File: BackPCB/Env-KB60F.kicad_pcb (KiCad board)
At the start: 2 copper layers, 283 x 126.5 mm, 9 parts

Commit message: Moved MCU lower to allow for mount hole to fit properly, Generated Gerber and bottom plate Gerber
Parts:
- G***: moved to B.Cu
- moved H11 1.75 mm to (353.1, 36.5)
- turned G*** to 180 degrees
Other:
- net class DIFF removed
- net class USB added: clearance 0.2, trace_width 0.25, via_dia 0.8, via_drill 0.4
- board text added: "Envious.Media"
- board text removed: "Envious.Media 2021"
- board text removed: "http://github.com/envious-data/env-kb60f"

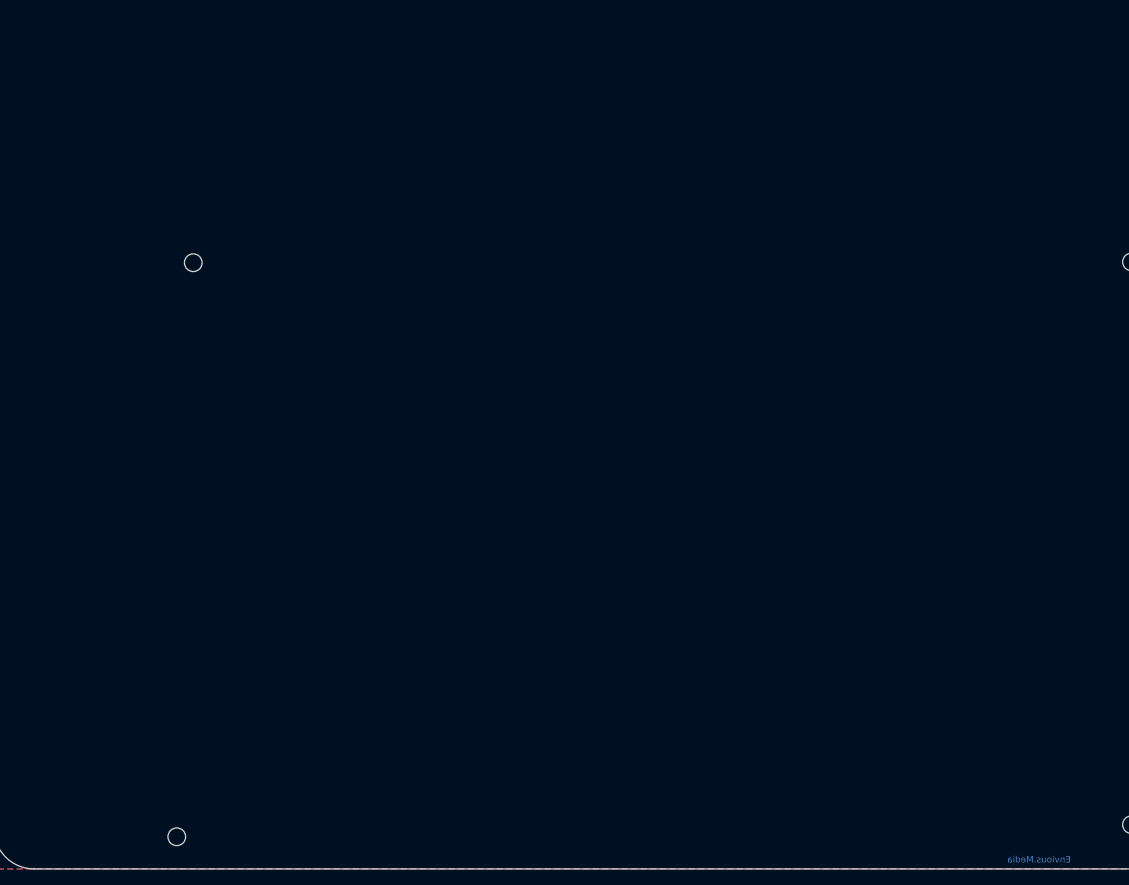
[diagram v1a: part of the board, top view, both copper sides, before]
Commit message: Corrected silkscreen, Generated updated Gerbers
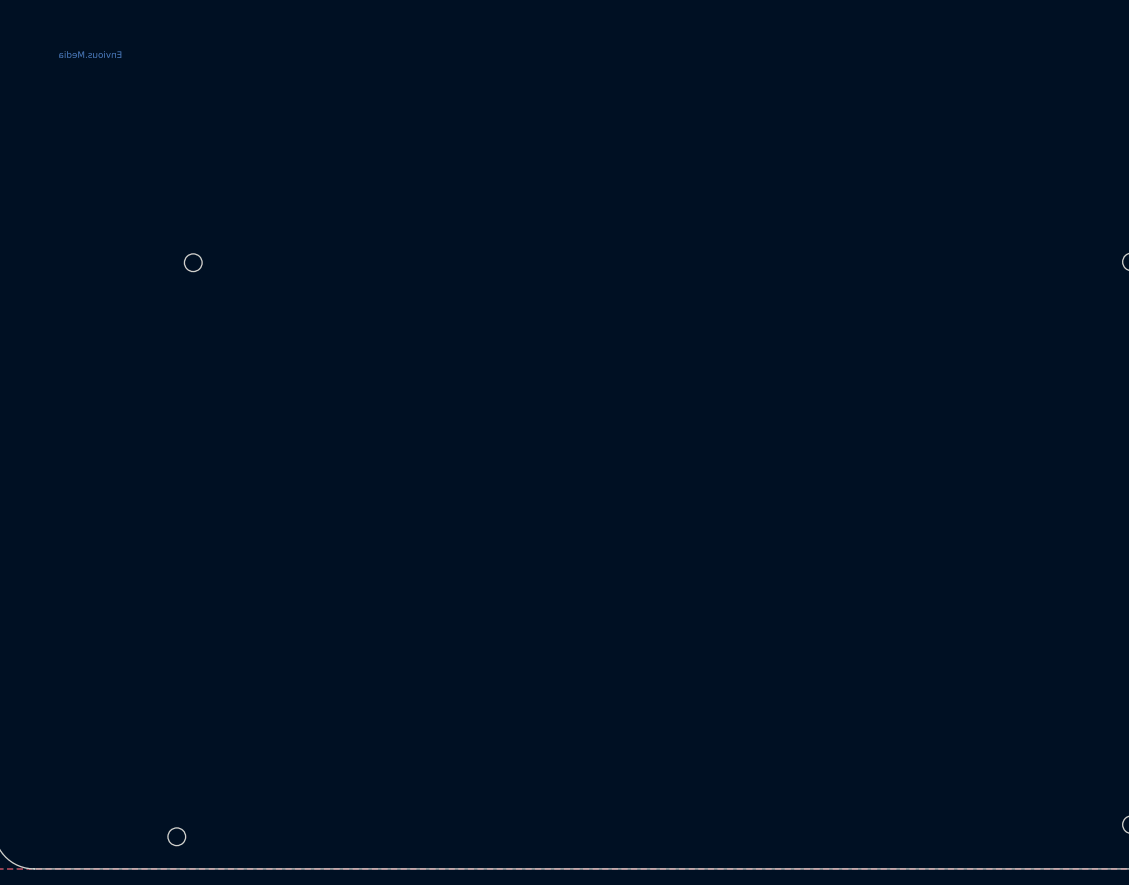
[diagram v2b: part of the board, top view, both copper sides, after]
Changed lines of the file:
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@@
     (pcbplotparams
       (layerselection 0x010fc_ffffffff)
-      (usegerberextensions false)
+      (usegerberextensions true)
       (usegerberattributes false)
       (usegerberadvancedattributes false)
@@
       (plotinvisibletext false)
       (padsonsilk false)
-      (subtractmaskfromsilk false)
+      (subtractmaskfromsilk true)
       (outputformat 1)
       (mirror false)
@@
     (effects (font (size 1.75 1.75) (thickness 0.15)) (justify mirror))
   )
-  (gr_text Envious.Media (at 207 158.325) (layer B.Cu)
+  (gr_text Envious.Media (at 89 58.25) (layer B.Cu)
     (effects (font (size 0.8 0.8) (thickness 0.15)) (justify mirror))
   )

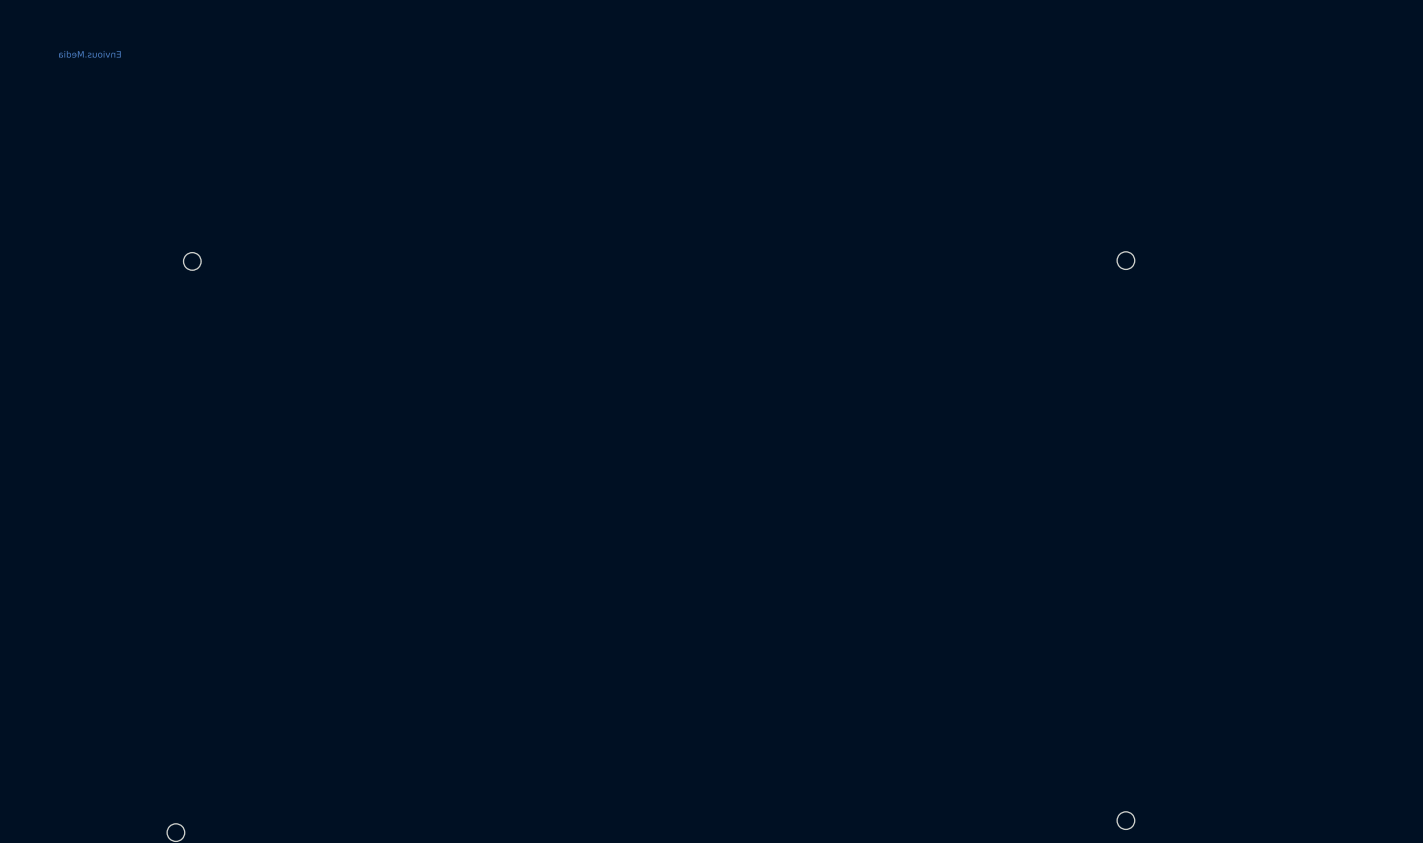
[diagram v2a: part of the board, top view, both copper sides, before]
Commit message: fixed backplate's ground fill and added a center logo on the rear of it.
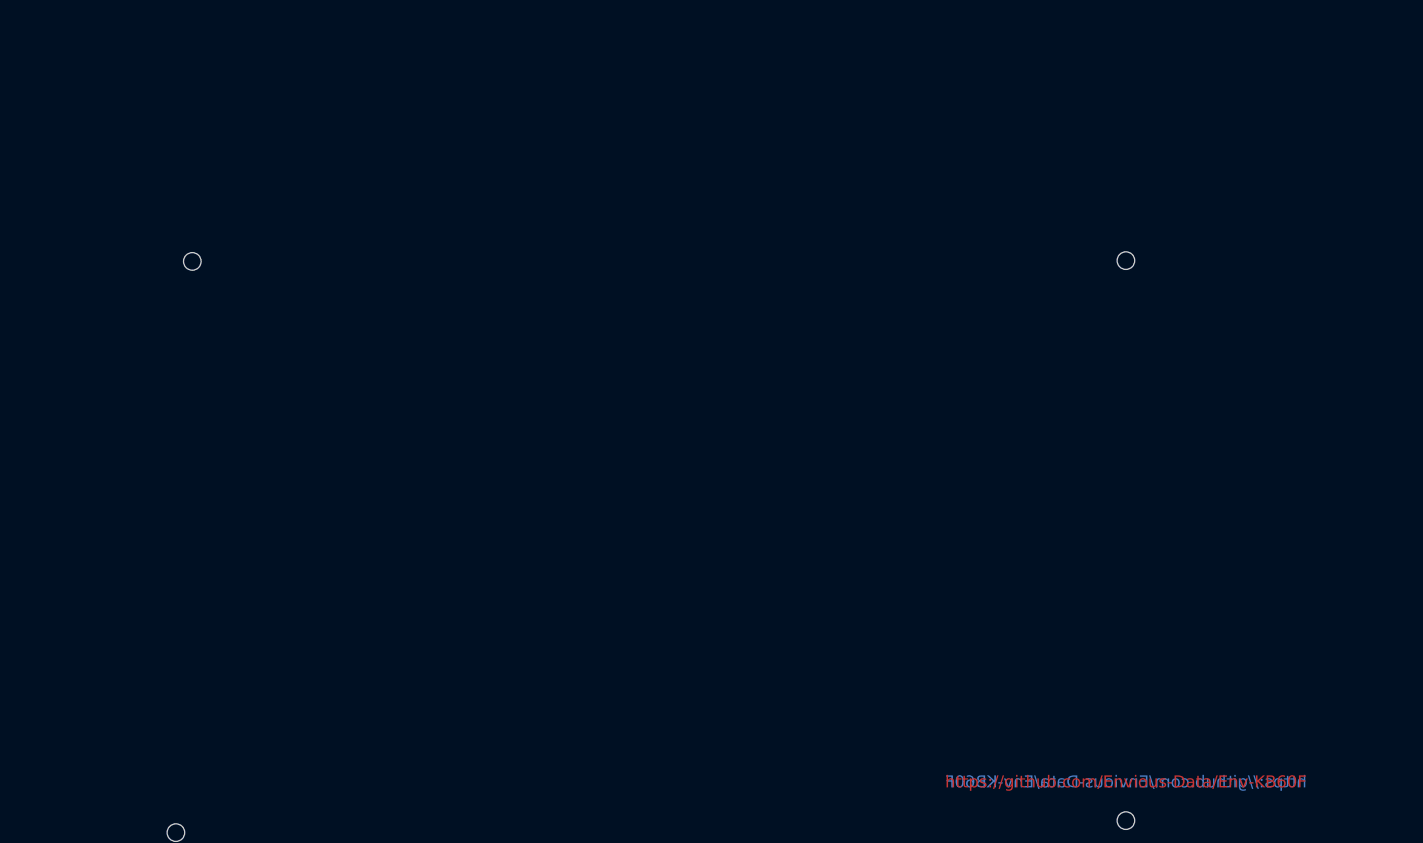
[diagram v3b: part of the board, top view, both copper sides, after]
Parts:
- removed the G*** at (87.2, 47.5)
- added G***: LOGO, Logo:logo, B.Cu at (218.5, 92.3)
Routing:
- added copper zone on B.Cu, net (none)
- added copper zone on F.Cu, net (none)
- removed copper zone on B.Cu, net GND
- removed copper zone on F.Cu, net GND
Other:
- board text added: "https://github.com/Envious-Data/Env-KB60F"
- board text removed: "Env-KB60F"
- board text removed: "Envious.Media"

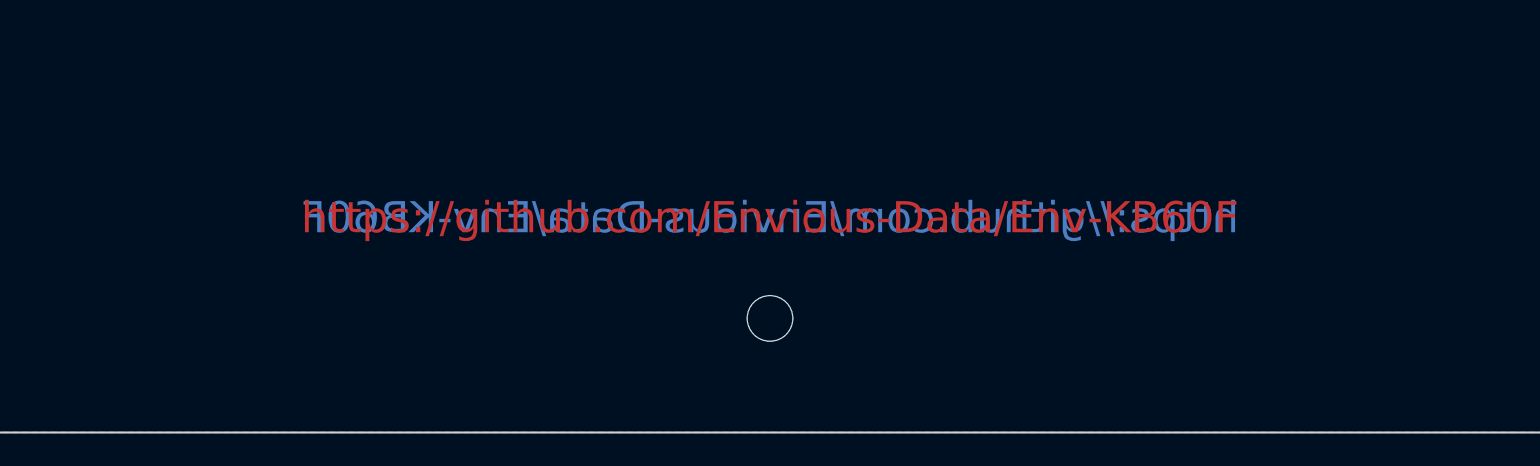
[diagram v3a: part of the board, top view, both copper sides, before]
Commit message: reorganize folder/files, added triple spacebar
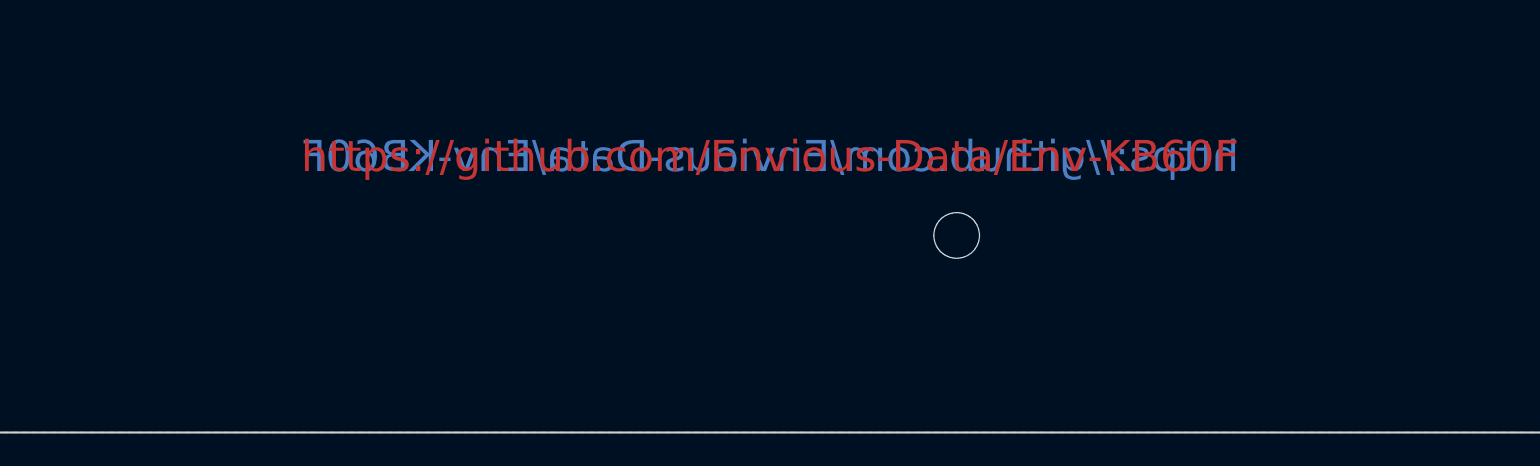
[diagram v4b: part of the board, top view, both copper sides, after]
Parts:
- moved H1 9.85 mm to (227.5, 150.0)

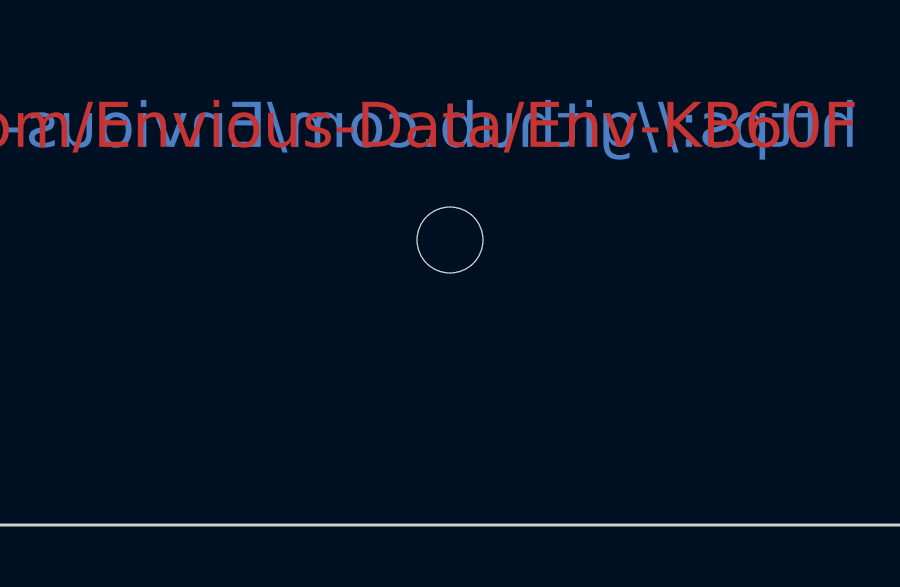
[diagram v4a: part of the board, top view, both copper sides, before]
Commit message: Corrected mount hole placement on all PCBs and updated the switch plate to fit triple spacebar split.
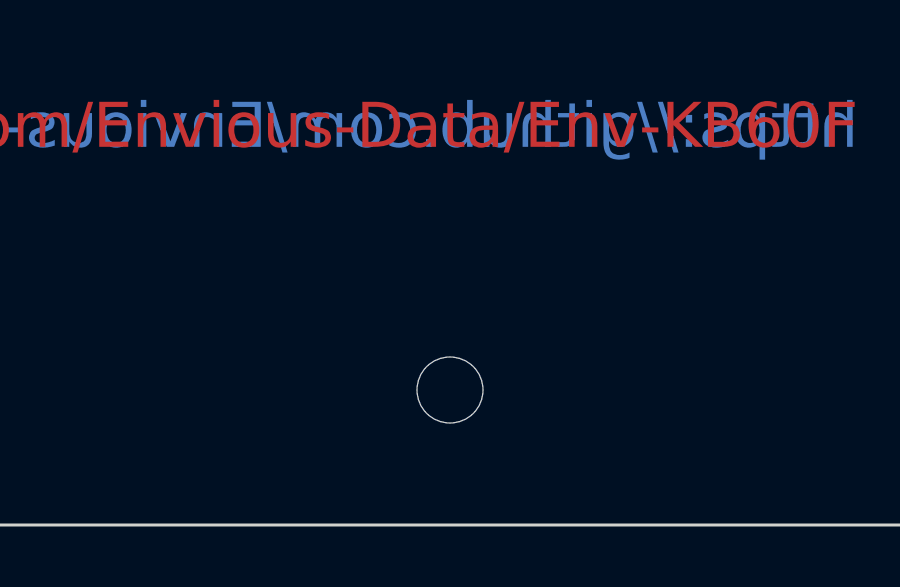
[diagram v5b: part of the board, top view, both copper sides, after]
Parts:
- moved H1 5.00 mm to (227.5, 155.0)
